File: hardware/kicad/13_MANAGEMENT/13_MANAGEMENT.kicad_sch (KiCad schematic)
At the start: 0 parts

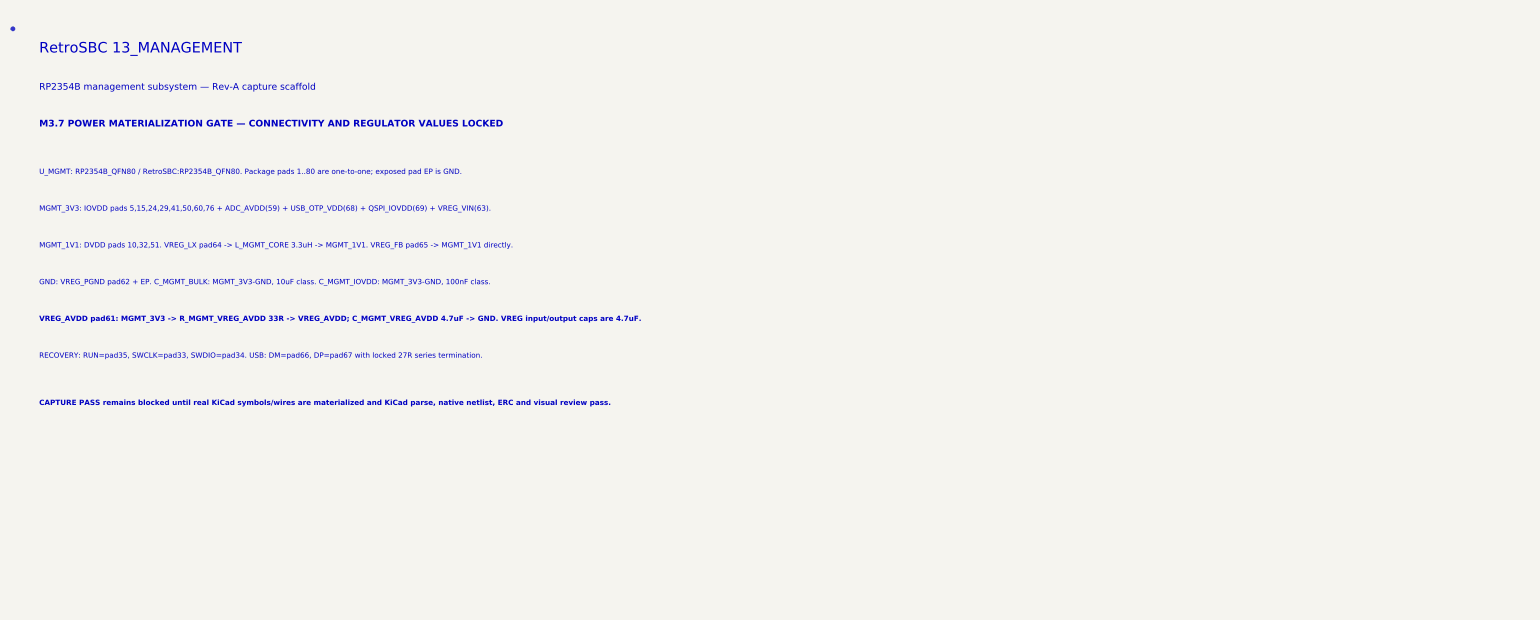
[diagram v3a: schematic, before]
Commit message: M3.7: materialize native U_MGMT symbol instance
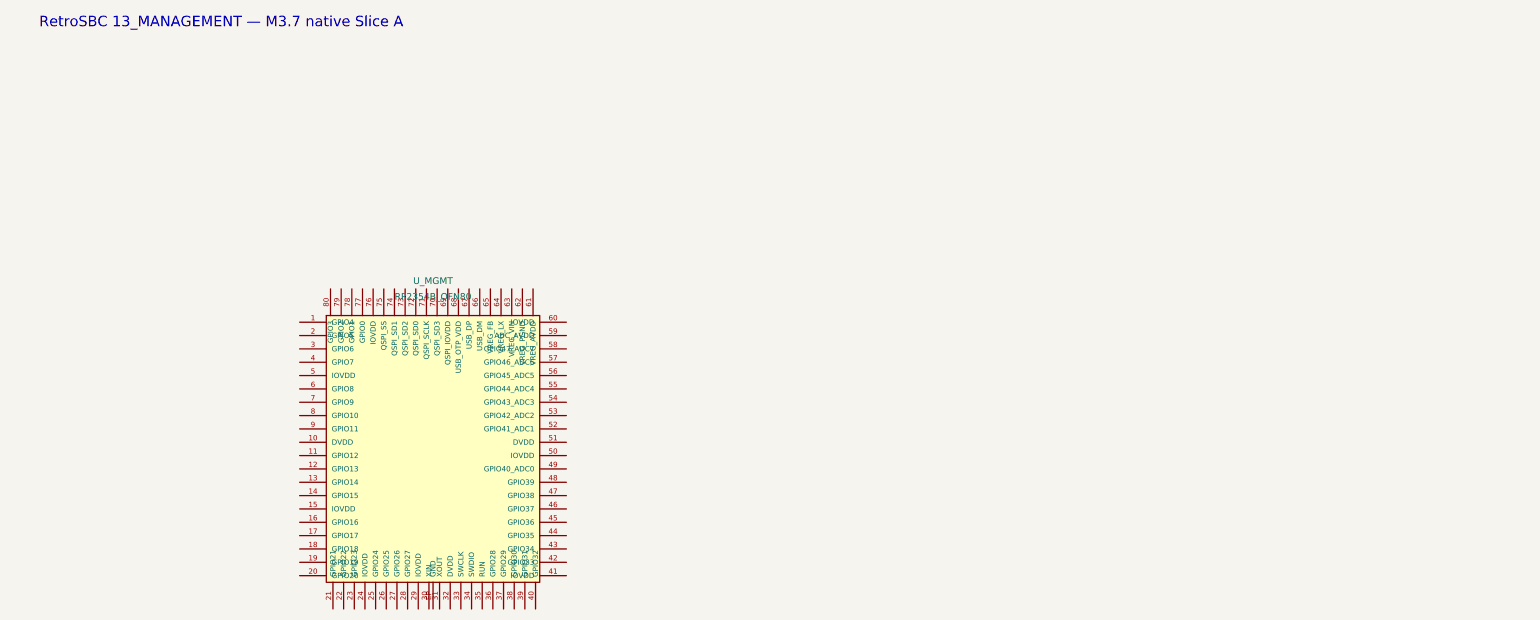
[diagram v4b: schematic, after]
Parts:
- added U_MGMT: RP2354B_QFN80, RetroSBC:RP2354B_QFN80, symbol RetroSBC-management:RP2354B_QFN80
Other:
- note added: "RetroSBC 13_MANAGEMENT — M3.7 native Slice A"
- note removed: "CAPTURE PASS remains blocked until real KiCad symbols/wires are materialized and KiCad parse, native netlist, ERC and visual review pass."
- note removed: "GND: VREG_PGND pad62 + EP. C_MGMT_BULK: MGMT_3V3-GND, 10uF class. C_MGMT_IOVDD: MGMT_3V3-GND, 100nF class."
- note removed: "M3.7 POWER MATERIALIZATION GATE — CONNECTIVITY AND REGULATOR VALUES LOCKED"
- note removed: "MGMT_1V1: DVDD pads 10,32,51. VREG_LX pad64 -> L_MGMT_CORE 3.3uH -> MGMT_1V1. VREG_FB pad65 -> MGMT_1V1 directly."
- note removed: "MGMT_3V3: IOVDD pads 5,15,24,29,41,50,60,76 + ADC_AVDD(59) + USB_OTP_VDD(68) + QSPI_IOVDD(69) + VREG_VIN(63)."
- note removed: "RECOVERY: RUN=pad35, SWCLK=pad33, SWDIO=pad34. USB: DM=pad66, DP=pad67 with locked 27R series termination."
- note removed: "RP2354B management subsystem — Rev-A capture scaffold"
- note removed: "RetroSBC 13_MANAGEMENT"
- note removed: "U_MGMT: RP2354B_QFN80 / RetroSBC:RP2354B_QFN80. Package pads 1..80 are one-to-one; exposed pad EP is GND."
- note removed: "VREG_AVDD pad61: MGMT_3V3 -> R_MGMT_VREG_AVDD 33R -> VREG_AVDD; C_MGMT_VREG_AVDD 4.7uF -> GND. VREG input/output caps are 4.7uF."
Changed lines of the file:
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@@
-(kicad_sch (version 20231120) (generator eeschema)
+(kicad_sch (version 20231120) (generator retrosbc_native_slice_a)
   (paper "A4")
-  (junction (at 20 20) (diameter 0) (color 0 0 0 0))
-  (text "RetroSBC 13_MANAGEMENT" (exclude_from_sim no) (at 25 25 0)
+  (text "RetroSBC 13_MANAGEMENT — M3.7 native Slice A" (exclude_from_sim no) (at 25 20 0)
     (effects (font (size 2 2) (thickness 0.3)) (justify left bottom)))
-  (text "RP2354B management subsystem — Rev-A capture scaffold" (exclude_from_sim no) (at 25 32 0)
-    (effects (font (size 1.27 1.27)) (justify left bottom)))
-  (text "M3.7 POWER MATERIALIZATION GATE — CONNECTIVITY AND REGULATOR VALUES LOCKED" (exclude_from_sim no) (at 25 39 0)
-    (effects (font (size 1.27 1.27) (bold yes)) (justify left bottom)))
-  (text "U_MGMT: RP2354B_QFN80 / RetroSBC:RP2354B_QFN80. Package pads 1..80 are one-to-one; exposed pad EP is GND." (exclude_from_sim no) (at 25 48 0)
-    (effects (font (size 1.0 1.0)) (justify left bottom)))
-  (text "MGMT_3V3: IOVDD pads 5,15,24,29,41,50,60,76 + ADC_AVDD(59) + USB_OTP_VDD(68) + QSPI_IOVDD(69) + VREG_VIN(63)." (exclude_from_sim no) (at 25 55 0)
-    (effects (font (size 1.0 1.0)) (justify left bottom)))
-  (text "MGMT_1V1: DVDD pads 10,32,51. VREG_LX pad64 -> L_MGMT_CORE 3.3uH -> MGMT_1V1. VREG_FB pad65 -> MGMT_1V1 directly." (exclude_from_sim no) (at 25 62 0)
-    (effects (font (size 1.0 1.0)) (justify left bottom)))
-  (text "GND: VREG_PGND pad62 + EP. C_MGMT_BULK: MGMT_3V3-GND, 10uF class. C_MGMT_IOVDD: MGMT_3V3-GND, 100nF class." (exclude_from_sim no) (at 25 69 0)
-    (effects (font (size 1.0 1.0)) (justify left bottom)))
-  (text "VREG_AVDD pad61: MGMT_3V3 -> R_MGMT_VREG_AVDD 33R -> VREG_AVDD; C_MGMT_VREG_AVDD 4.7uF -> GND. VREG input/output caps are 4.7uF." (exclude_from_sim no) (at 25 76 0)
-    (effects (font (size 1.0 1.0) (bold yes)) (justify left bottom)))
-  (text "RECOVERY: RUN=pad35, SWCLK=pad33, SWDIO=pad34. USB: DM=pad66, DP=pad67 with locked 27R series termination." (exclude_from_sim no) (at 25 83 0)
-    (effects (font (size 1.0 1.0)) (justify left bottom)))
-  (text "CAPTURE PASS remains blocked until real KiCad symbols/wires are materialized and KiCad parse, native netlist, ERC and visual review pass." (exclude_from_sim no) (at 25 92 0)
-    (effects (font (size 1.0 1.0) (bold yes)) (justify left bottom)))
+  (symbol (lib_id "RetroSBC-management:RP2354B_QFN80") (at 100 100 0) (unit 1)
+    (exclude_from_sim no) (in_bom yes) (on_board yes)
+    (property "Reference" "U_MGMT" (at 100 68 0) (effects (font (size 1.27 1.27))))
+    (property "Value" "RP2354B_QFN80" (at 100 71 0) (effects (font (size 1.27 1.27))))
+    (property "Footprint" "RetroSBC:RP2354B_QFN80" (at 100 100 0) (effects (font (size 1.27 1.27)) hide))
+    (property "Datasheet" "RP2350 datasheet" (at 100 100 0) (effects (font (size 1.27 1.27)) hide))
+    (property "Description" "RP2354B management MCU" (at 100 100 0) (effects (font (size 1.27 1.27)) hide))
+    (pin "1")
+    (pin "2")
+    (pin "3")
+    (pin "4")
+    (pin "5")
+    (pin "6")
+    (pin "7")
+    (pin "8")
+    (pin "9")
+    (pin "10")
+    (pin "11")
+    (pin "12")
+    (pin "13")
+    (pin "14")
+    (pin "15")
+    (pin "16")
+    (pin "17")
+    (pin "18")
+    (pin "19")
+    (pin "20")
+    (pin "21")
+    (pin "22")
+    (pin "23")
+    (pin "24")
+    (pin "25")
+    (pin "26")
+    (pin "27")
+    (pin "28")
+    (pin "29")
+    (pin "30")
+    (pin "31")
+    (pin "32")
+    (pin "33")
+    (pin "34")
+    (pin "35")
+    (pin "36")
+    (pin "37")
+    (pin "38")
+    (pin "39")
+    (pin "40")
+    (pin "41")
+    (pin "42")
+    (pin "43")
+    (pin "44")
+    (pin "45")
+    (pin "46")
+    (pin "47")
+    (pin "48")
+    (pin "49")
+    (pin "50")
+    (pin "51")
+    (pin "52")
+    (pin "53")
+    (pin "54")
+    (pin "55")
+    (pin "56")
+    (pin "57")
+    (pin "58")
+    (pin "59")
+    (pin "60")
+    (pin "61")
+    (pin "62")
+    (pin "63")
+    (pin "64")
+    (pin "65")
+    (pin "66")
+    (pin "67")
+    (pin "68")
+    (pin "69")
+    (pin "70")
+    (pin "71")
+    (pin "72")
+    (pin "73")
+    (pin "74")
+    (pin "75")
+    (pin "76")
+    (pin "77")
+    (pin "78")
+    (pin "79")
+    (pin "80")
+    (pin "EP")
+    (instances (project "RetroSBC-13-MANAGEMENT"
+      (path "/7a5d3d51-9e2f-4d31-b7cb-9fbd10b8c301/11111111-1111-4111-8111-111111111111" (reference "U_MGMT") (unit 1))
+    ))
+  )
   (sheet_instances (path "/" (page "1")))
 )
